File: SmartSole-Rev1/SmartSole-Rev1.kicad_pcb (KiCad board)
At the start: 2 copper layers, 37.4 x 68.6 mm, 33 parts, among them J1 5103310-5, J2 1-825433-2, J3 1-825433-2, U1 MCP6004, U2 MCP6004, U3 AD1583

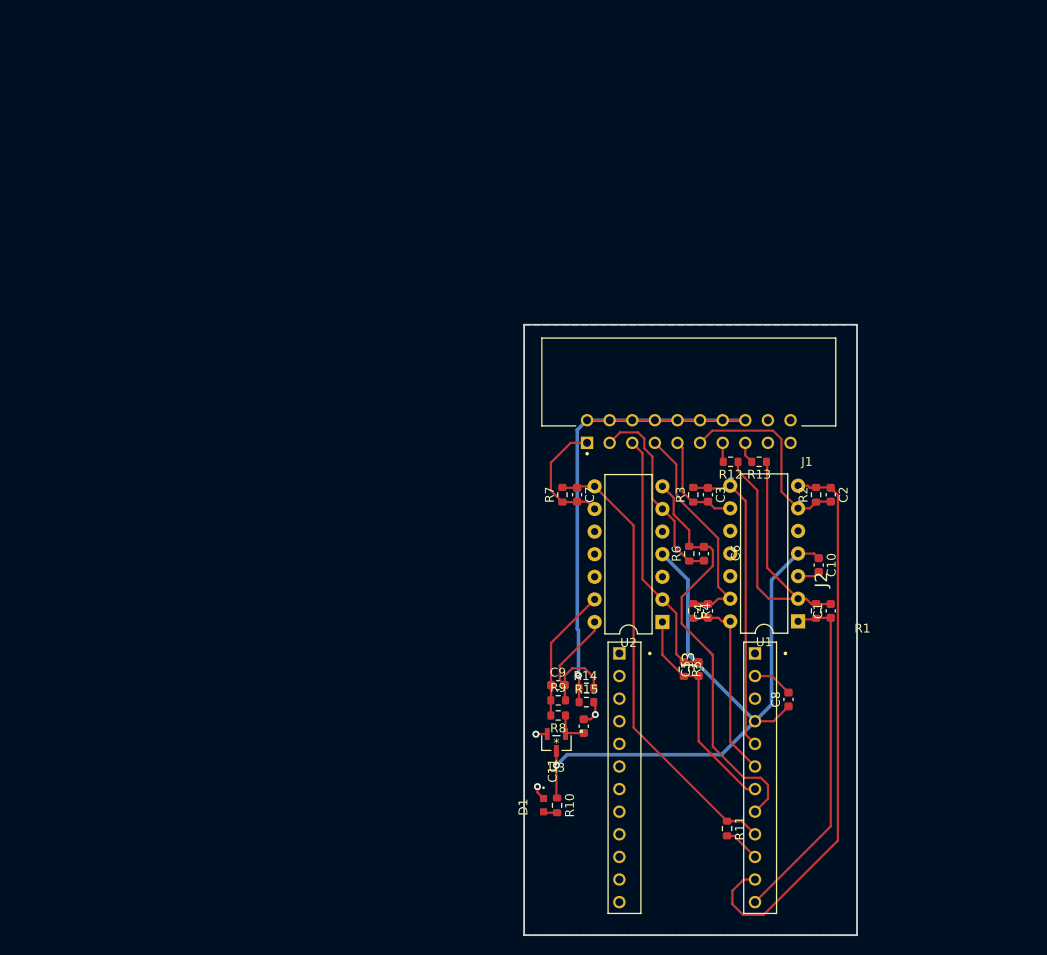
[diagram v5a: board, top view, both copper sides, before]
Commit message: Moved component ref silk screen, added board stackup + characteristics
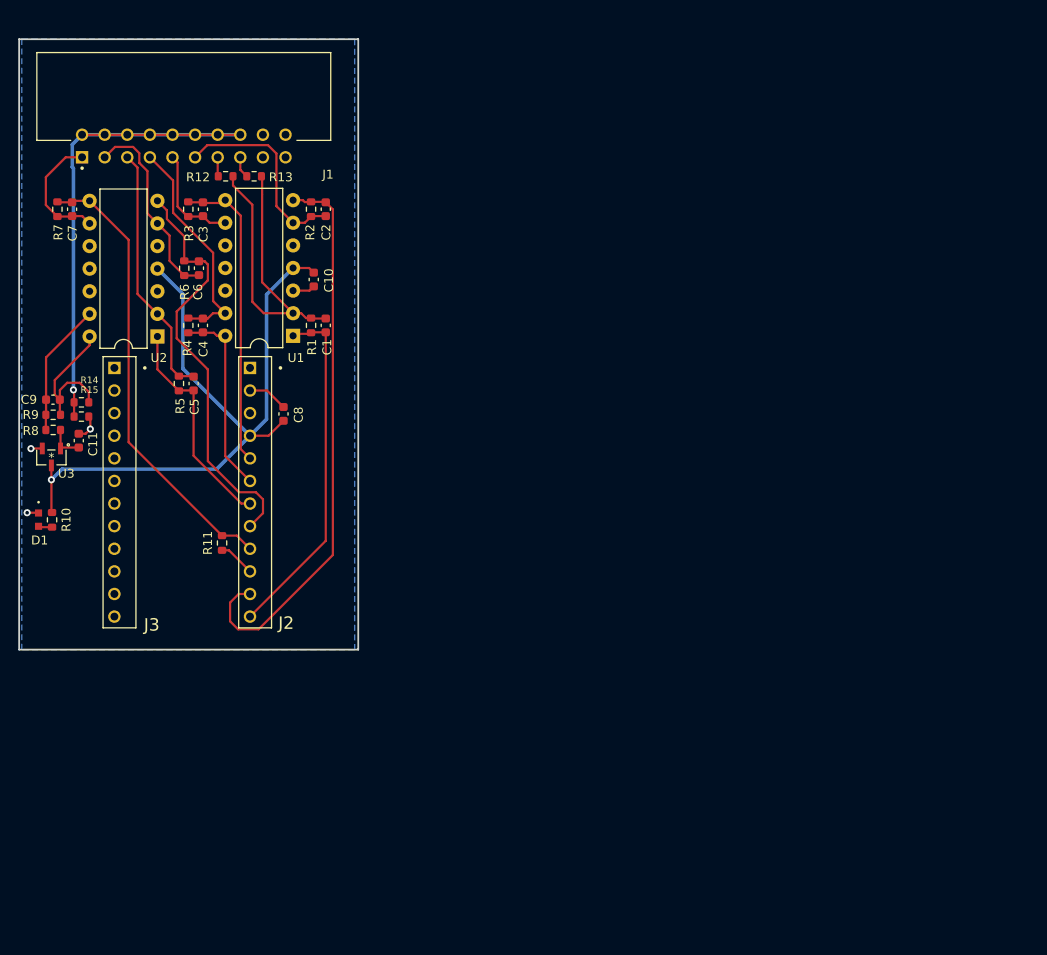
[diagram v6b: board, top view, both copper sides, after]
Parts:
- moved C10 65.2 mm to (92.7, 58.3)
- moved C7 65.2 mm to (65.5, 50.4)
- moved J1 65.2 mm to (78.1, 43.3)
- moved R2 65.2 mm to (92.4, 50.4)
- moved C1 65.2 mm to (94.0, 63.5)
- moved C11 65.2 mm to (66.3, 76.4)
- moved C2 65.2 mm to (94.0, 50.4)
- moved C3 65.2 mm to (80.2, 50.4)
- moved C4 65.2 mm to (80.2, 63.5)
- moved C6 65.2 mm to (79.8, 57.0)
- moved C8 65.2 mm to (89.3, 73.4)
- moved C9 65.2 mm to (63.4, 71.8)
- moved J2 65.2 mm to (85.5, 82.2)
- moved J3 65.2 mm to (70.3, 82.2)
- moved R1 65.2 mm to (92.4, 63.5)
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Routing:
- net /ForceIn_4: track 26.6 -> 25.4 mm
- net /AIN5: track 48.0 -> 47.4 mm
- net GND: track 12.9 -> 12.4 mm
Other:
- board size 37.4 x 68.6 mm -> 38.1 x 68.6 mm
- board text added: "0"
- board text added: "0 mils"
- board text added: "0.02"
- board text added: "0.3937008 mils"
- board text added: "1"
- board text added: "1.377953 mils"
- board text added: "11.81 mils"
- board text added: "1507.87 mils x 2707.87 mils"
- board text added: "2"
- board text added: "3.3"
- board text added: "4.5"
- board text added: "59.44882 mils"
- board text added: "6.00 mils / 6.00 mils"
- board text added: "62.99 mils"
- board text added: "B.Cu"
- board text added: "B.Mask"
- board text added: "B.Paste"
- board text added: "B.Silkscreen"
- board text added: "BOARD CHARACTERISTICS"
- board text added: "Board Thickness:"
- board text added: "Board overall dimensions:"
- board text added: "Bottom Silk Screen"
- board text added: "Bottom Solder Mask"
- board text added: "Bottom Solder Paste"
- board text added: "Castellated pads:"
- board text added: "Color"
- board text added: "Copper Finish:"
- board text added: "Copper Layer Count:"
- board text added: "Dielectric 1"
- board text added: "Edge card connectors:"
- board text added: "Epsilon R"
- board text added: "F.Cu"
- board text added: "F.Mask"
- board text added: "F.Paste"
- board text added: "F.Silkscreen"
- board text added: "FR4"
- board text added: "Impedance Control:"
- board text added: "Layer Name"
- board text added: "Loss Tangent"
- board text added: "Material"
- board text added: "Min hole diameter:"
- board text added: "Min track/spacing:"
- board text added: "No"
- board text added: "None"
- board text added: "Not specified"
- board text added: "Plated Board Edge:"
- board text added: "Thickness (mils)"
- board text added: "Top Silk Screen"
- board text added: "Top Solder Mask"
- board text added: "Top Solder Paste"
- board text added: "Type"
- board text added: "copper"
- board text added: "core"

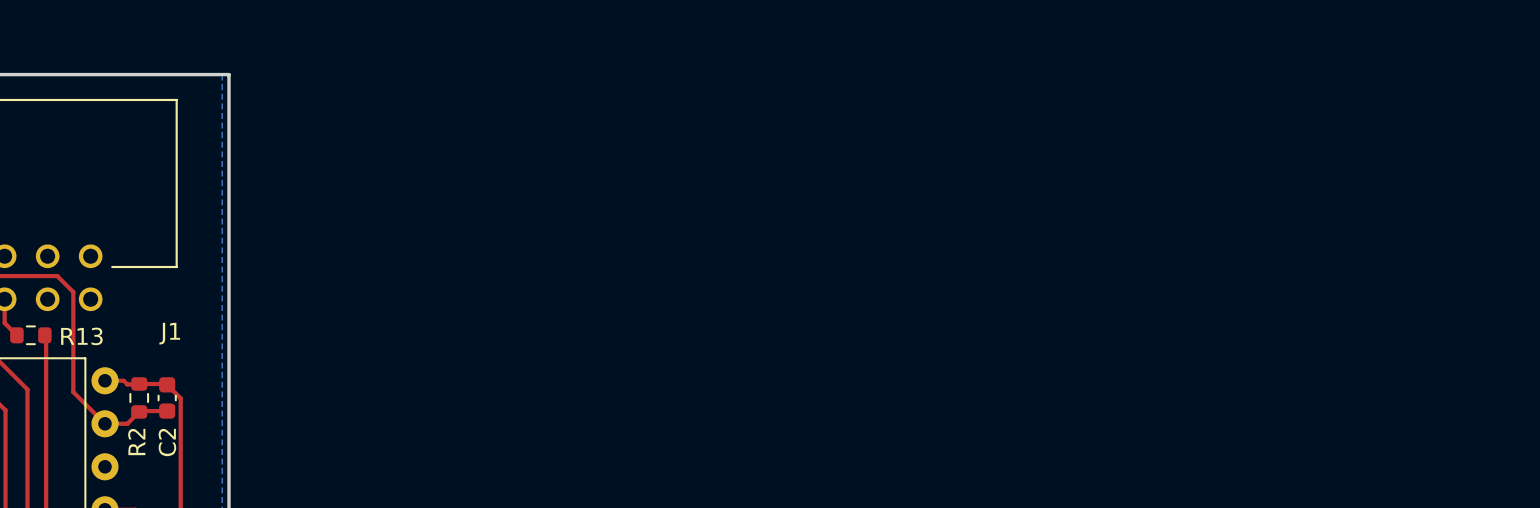
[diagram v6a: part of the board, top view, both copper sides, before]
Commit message: changed to non-inverting config
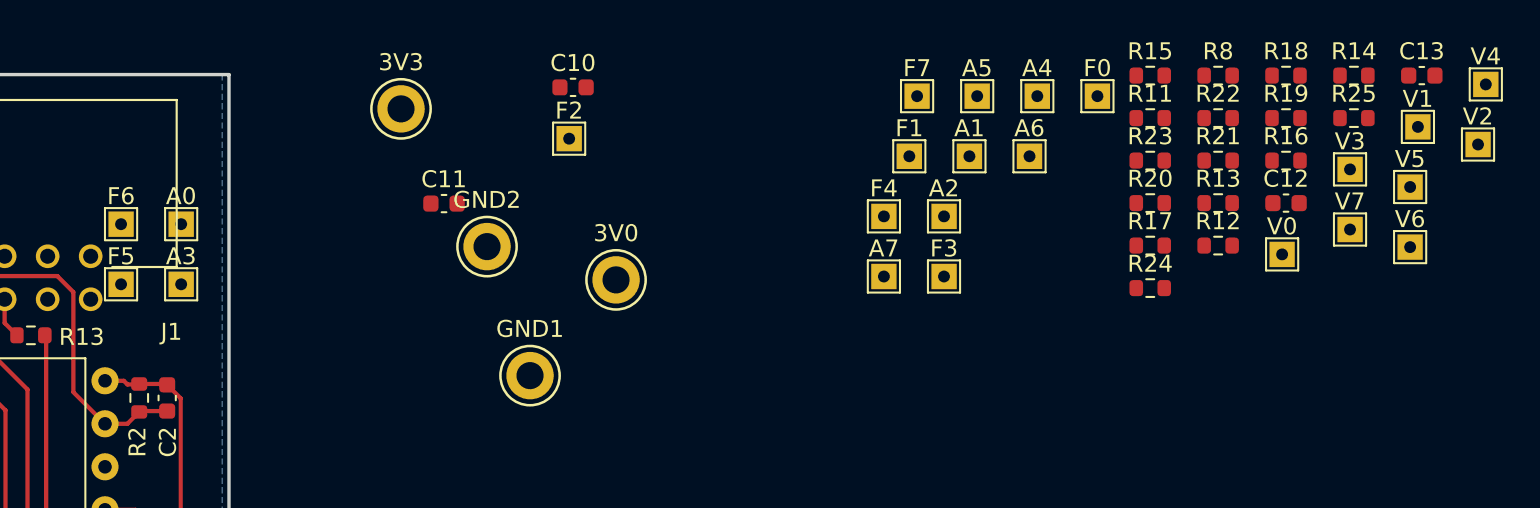
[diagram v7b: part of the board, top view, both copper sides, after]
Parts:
- added 3V0: 5005, TestPoint:TestPoint_Keystone_5005-5009_Compact, F.Cu at (120.5, 43.4)
- added 3V3: 5005, TestPoint:TestPoint_Keystone_5005-5009_Compact, F.Cu at (107.8, 33.3)
- added A0: TestPoint_Small, TestPoint:TestPoint_THTPad_1.5x1.5mm_Drill0.7mm, F.Cu at (94.8, 40.2)
- added A1: TestPoint_Small, TestPoint:TestPoint_THTPad_1.5x1.5mm_Drill0.7mm, F.Cu at (141.4, 36.1)
- added A2: TestPoint_Small, TestPoint:TestPoint_THTPad_1.5x1.5mm_Drill0.7mm, F.Cu at (139.9, 39.7)
- added A3: TestPoint_Small, TestPoint:TestPoint_THTPad_1.5x1.5mm_Drill0.7mm, F.Cu at (94.8, 43.7)
- added A4: TestPoint_Small, TestPoint:TestPoint_THTPad_1.5x1.5mm_Drill0.7mm, F.Cu at (145.4, 32.6)
- added A5: TestPoint_Small, TestPoint:TestPoint_THTPad_1.5x1.5mm_Drill0.7mm, F.Cu at (141.9, 32.6)
- added A6: TestPoint_Small, TestPoint:TestPoint_THTPad_1.5x1.5mm_Drill0.7mm, F.Cu at (144.9, 36.1)
- added A7: TestPoint_Small, TestPoint:TestPoint_THTPad_1.5x1.5mm_Drill0.7mm, F.Cu at (136.3, 43.2)
- added C10: 4.7uF, Capacitor_SMD:C_0603_1608Metric, F.Cu at (118.0, 32.1)
- added C11: 1uF, Capacitor_SMD:C_0603_1608Metric, F.Cu at (110.4, 38.9)
- added C12: 0.1uF, Capacitor_SMD:C_0603_1608Metric, F.Cu at (160.1, 38.9)
- added C13: 0.1uF, Capacitor_SMD:C_0603_1608Metric, F.Cu at (168.1, 31.4)
- added F0: TestPoint_Small, TestPoint:TestPoint_THTPad_1.5x1.5mm_Drill0.7mm, F.Cu at (149.0, 32.6)
- added F1: TestPoint_Small, TestPoint:TestPoint_THTPad_1.5x1.5mm_Drill0.7mm, F.Cu at (137.8, 36.1)
- added F2: TestPoint_Small, TestPoint:TestPoint_THTPad_1.5x1.5mm_Drill0.7mm, F.Cu at (117.8, 35.1)
- added F3: TestPoint_Small, TestPoint:TestPoint_THTPad_1.5x1.5mm_Drill0.7mm, F.Cu at (139.9, 43.2)
- added F4: TestPoint_Small, TestPoint:TestPoint_THTPad_1.5x1.5mm_Drill0.7mm, F.Cu at (136.3, 39.7)
- added F5: TestPoint_Small, TestPoint:TestPoint_THTPad_1.5x1.5mm_Drill0.7mm, F.Cu at (91.3, 43.7)
- added F6: TestPoint_Small, TestPoint:TestPoint_THTPad_1.5x1.5mm_Drill0.7mm, F.Cu at (91.3, 40.2)
- added F7: TestPoint_Small, TestPoint:TestPoint_THTPad_1.5x1.5mm_Drill0.7mm, F.Cu at (138.3, 32.6)
- added GND1: 5006, TestPoint:TestPoint_Keystone_5005-5009_Compact, F.Cu at (115.4, 49.1)
- added GND2: 5006, TestPoint:TestPoint_Keystone_5005-5009_Compact, F.Cu at (112.9, 41.5)
- added R11: R, Resistor_SMD:R_0603_1608Metric, F.Cu at (152.1, 33.9)
- added R12: R, Resistor_SMD:R_0603_1608Metric, F.Cu at (156.1, 41.4)
- added R13: R, Resistor_SMD:R_0603_1608Metric, F.Cu at (156.1, 38.9)
- added R14: R, Resistor_SMD:R_0603_1608Metric, F.Cu at (164.1, 31.4)
- added R15: R, Resistor_SMD:R_0603_1608Metric, F.Cu at (152.1, 31.4)
- added R16: R, Resistor_SMD:R_0603_1608Metric, F.Cu at (160.1, 36.4)
- added R17: R, Resistor_SMD:R_0603_1608Metric, F.Cu at (152.1, 41.4)
- added R18: R, Resistor_SMD:R_0603_1608Metric, F.Cu at (160.1, 31.4)
- added R19: R, Resistor_SMD:R_0603_1608Metric, F.Cu at (160.1, 33.9)
- added R20: R, Resistor_SMD:R_0603_1608Metric, F.Cu at (152.1, 38.9)
- added R21: R, Resistor_SMD:R_0603_1608Metric, F.Cu at (156.1, 36.4)
- added R22: R, Resistor_SMD:R_0603_1608Metric, F.Cu at (156.1, 33.9)
- added R23: R, Resistor_SMD:R_0603_1608Metric, F.Cu at (152.1, 36.4)
- added R24: R, Resistor_SMD:R_0603_1608Metric, F.Cu at (152.1, 43.9)
- added R25: R, Resistor_SMD:R_0603_1608Metric, F.Cu at (164.1, 33.9)
- added R8: R, Resistor_SMD:R_0603_1608Metric, F.Cu at (156.1, 31.4)
- added V0: TestPoint_Small, TestPoint:TestPoint_THTPad_1.5x1.5mm_Drill0.7mm, F.Cu at (159.9, 41.9)
- added V1: TestPoint_Small, TestPoint:TestPoint_THTPad_1.5x1.5mm_Drill0.7mm, F.Cu at (167.9, 34.4)
- added V2: TestPoint_Small, TestPoint:TestPoint_THTPad_1.5x1.5mm_Drill0.7mm, F.Cu at (171.4, 35.5)
- added V3: TestPoint_Small, TestPoint:TestPoint_THTPad_1.5x1.5mm_Drill0.7mm, F.Cu at (163.9, 36.9)
- added V4: TestPoint_Small, TestPoint:TestPoint_THTPad_1.5x1.5mm_Drill0.7mm, F.Cu at (171.9, 31.9)
- added V5: TestPoint_Small, TestPoint:TestPoint_THTPad_1.5x1.5mm_Drill0.7mm, F.Cu at (167.4, 38.0)
- added V6: TestPoint_Small, TestPoint:TestPoint_THTPad_1.5x1.5mm_Drill0.7mm, F.Cu at (167.4, 41.5)
- added V7: TestPoint_Small, TestPoint:TestPoint_THTPad_1.5x1.5mm_Drill0.7mm, F.Cu at (163.9, 40.5)
- C8: value 0.1u -> 1uF
- C9: value .01u -> 47pF
- R10: value 10k -> 68
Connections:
- C2 pad 2: /ForceIn_2 -> /ForceIn_1
- C3 pad 2: /ForceIn_3 -> /ForceIn_2
- C4 pad 2: /ForceIn_4 -> /ForceIn_3
- C5 pad 2: /ForceIn_5 -> /ForceIn_4
- C6 pad 2: /ForceIn_6 -> /ForceIn_5
- C7 pad 2: /ForceIn_7 -> /ForceIn_6
- C8 pad 1: /3.3V -> +3V3
- C9 pad 1: Net-(R8-Pad2) -> /ForceIn_7
- C9 pad 2: Net-(R9-Pad2) -> /AIN7
- J1 pad 10: /VRef -> GND
- J1 pad 12: /VRef -> GND
- J1 pad 13: Net-(J1-Pad13) -> /ForceIn_1
- J1 pad 14: /VRef -> GND
- J1 pad 15: Net-(J1-Pad15) -> /ForceIn_0
- J1 pad 16: /VRef -> GND
- J1 pad 17: unconnected-(J1-Pad17) -> GND
- J1 pad 18: unconnected-(J1-Pad18) -> GND
- J1 pad 19: unconnected-(J1-Pad19) -> GND
- J1 pad 2: /VRef -> GND
- J1 pad 20: unconnected-(J1-Pad20) -> GND
- J1 pad 4: /VRef -> GND
- J1 pad 6: /VRef -> GND
- J1 pad 8: /VRef -> GND
- J2 pad 10: Net-(J2-Pad10) -> /AIN7
- J2 pad 4: /3.3V -> +3V3
- R10 pad 1: /3.3V -> +3V3
- R2 pad 1: /ForceIn_2 -> /ForceIn_1
- R3 pad 1: /ForceIn_3 -> /ForceIn_2
- R4 pad 1: /ForceIn_4 -> /ForceIn_3
- R5 pad 1: /ForceIn_5 -> /ForceIn_4
- R6 pad 1: /ForceIn_6 -> /ForceIn_5
- R7 pad 1: /ForceIn_7 -> /ForceIn_6
- R9 pad 1: Net-(R8-Pad2) -> /ForceIn_7
- R9 pad 2: Net-(R9-Pad2) -> /AIN7
- U1 pad 10: GND -> /Op Amps/VRef2
- U1 pad 12: GND -> /Op Amps/VRef3
- U1 pad 13: /ForceIn_4 -> /ForceIn_3
- U1 pad 3: GND -> /Op Amps/VRef0
- U1 pad 4: /3.3V -> +3V3
- U1 pad 5: GND -> /Op Amps/VRef1
- U1 pad 6: /ForceIn_2 -> /ForceIn_1
- U1 pad 9: /ForceIn_3 -> /ForceIn_2
- U2 pad 10: GND -> /Op Amps/VRef6
- U2 pad 12: GND -> /Op Amps/VRef7
- U2 pad 13: Net-(R8-Pad2) -> /ForceIn_7
- U2 pad 14: Net-(R9-Pad2) -> /AIN7
- U2 pad 2: /ForceIn_5 -> /ForceIn_4
- U2 pad 3: GND -> /Op Amps/VRef4
- U2 pad 4: /3.3V -> +3V3
- U2 pad 5: GND -> /Op Amps/VRef5
- U2 pad 6: /ForceIn_6 -> /ForceIn_5
- U2 pad 9: /ForceIn_7 -> /ForceIn_6
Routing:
- net /3.3V: track 80.6 -> 0.00 mm, vias 1 -> 0
- net +3V3: track 0.00 -> 80.6 mm, vias 0 -> 1
- net /VRef: track 67.8 -> 0.00 mm
- net GND: track 12.4 -> 80.1 mm
- net /ForceIn_1: track 0.00 -> 22.6 mm
- net Net-(R9-Pad2): track 17.0 -> 0.00 mm
- net /AIN7: track 0.00 -> 17.0 mm
- net Net-(R8-Pad2): track 15.1 -> 0.00 mm
- net /ForceIn_3: track 11.8 -> 25.4 mm
- net /ForceIn_2: track 22.6 -> 11.8 mm
- net /ForceIn_6: track 22.2 -> 13.9 mm
- net /ForceIn_5: track 28.7 -> 22.2 mm
- net /ForceIn_4: track 25.4 -> 28.7 mm
- net /ForceIn_7: track 13.9 -> 15.1 mm

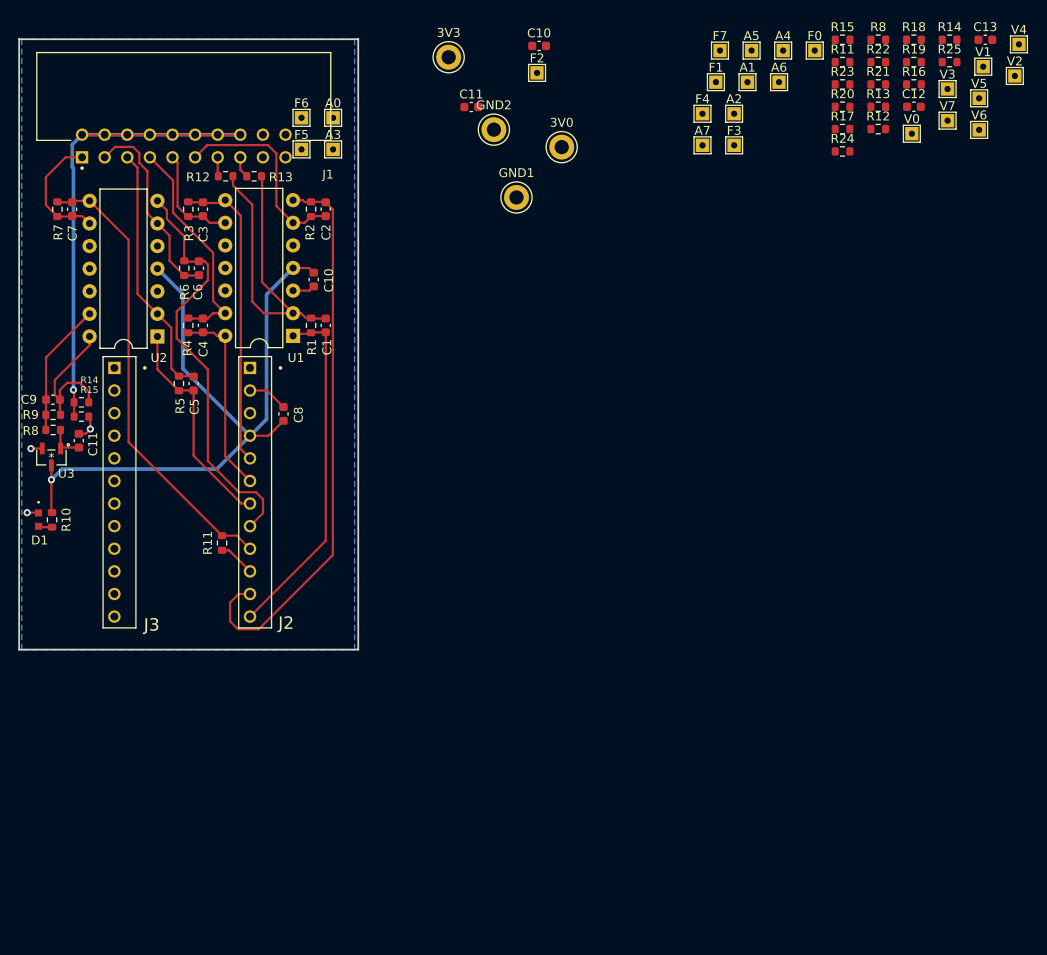
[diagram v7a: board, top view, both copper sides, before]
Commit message: changed to single coltage reference per opamp IC
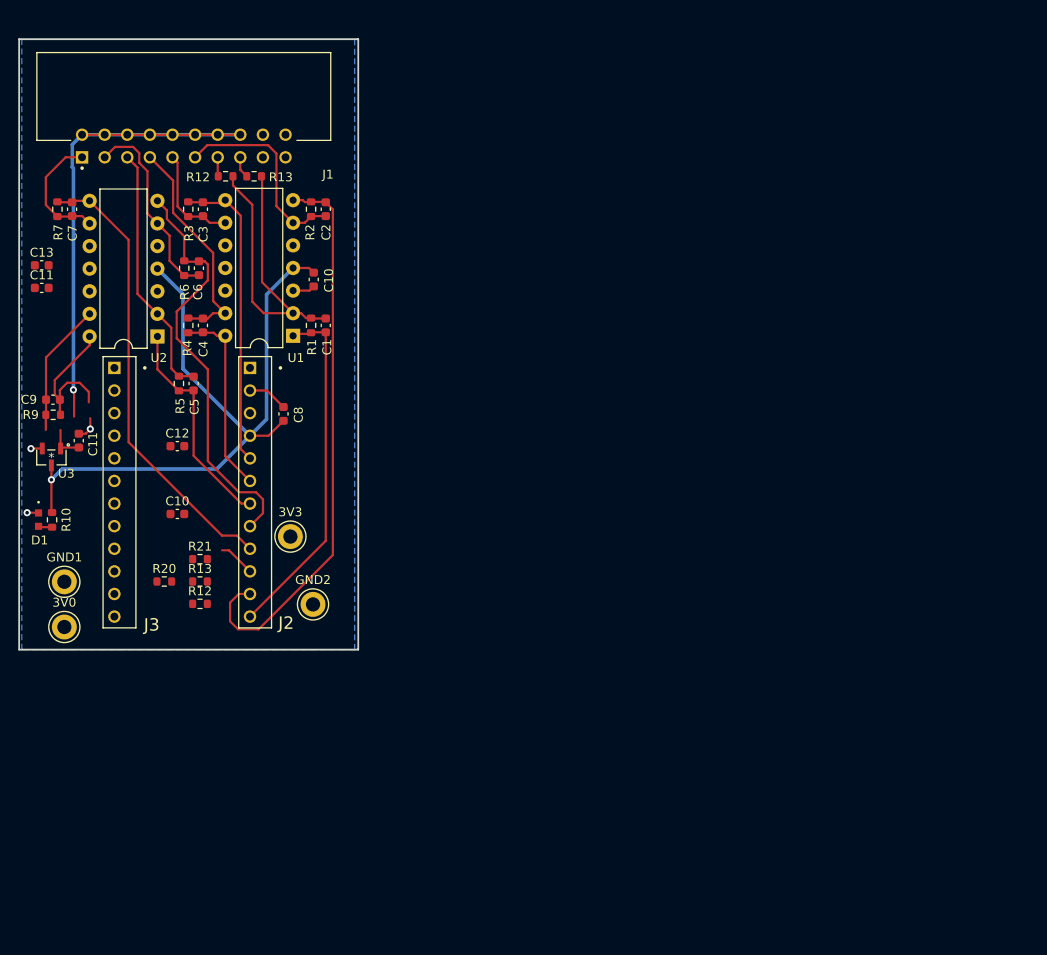
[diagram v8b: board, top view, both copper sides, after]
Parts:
- removed A0, A1, A2, A3, A4, A5, A6, A7, F0, F1, F2, F3, F4, F5, F6, F7, V0, V1, V2, V3, V4, V5, V6, V7: TestPoint_Small, TestPoint:TestPoint_THTPad_1.5x1.5mm_Drill0.7mm
- removed R11, R15: 0 - DNP, Resistor_SMD:R_0603_1608Metric
- removed R11, R14, R15, R16, R17, R18, R19, R22, R23, R24, R25, R8: R, Resistor_SMD:R_0603_1608Metric
- removed R14: 0, Resistor_SMD:R_0603_1608Metric
- removed R8: 680, Resistor_SMD:R_0603_1608Metric
- C10: value 4.7u -> 4.7uF
- C11: value 1u -> 1uF
- R12: value 0 -> R
- R13: value 0 - DNP -> R
- moved C13 109.0 mm to (62.1, 56.7)
- moved R12 93.0 mm to (79.9, 94.8)
- moved R13 93.0 mm to (79.9, 92.2)
- moved R21 93.0 mm to (79.9, 89.7)
- moved R20 93.0 mm to (75.9, 92.2)
- moved C12 91.1 mm to (77.3, 77.0)
- moved 3V0 77.6 mm to (64.6, 97.4)
- moved GND1 66.7 mm to (64.6, 92.3)
- moved C10 66.5 mm to (77.3, 84.7)
- moved GND2 57.1 mm to (92.6, 94.8)
- moved 3V3 56.7 mm to (90.0, 87.2)
- moved C11 52.4 mm to (62.1, 59.3)
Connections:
- C10 pad 1: /3.3V -> +3V3
- C11 pad 1: Net-(R8-Pad1) -> /VRef
- R12 pad 2: /Op Amps/VRef0 -> /Op Amps/VRef1
- R12 pad 1: /ForceIn_0 -> /VRef
- R12 pad 2: Net-(J1-Pad13) -> /Op Amps/VRef1
- R13 pad 1: /ForceIn_0 -> /Op Amps/VRef1
- R13 pad 2: Net-(J1-Pad15) -> GND
- R13 pad 1: /Op Amps/VRef0 -> /Op Amps/VRef1
- R20 pad 2: /Op Amps/VRef4 -> /Op Amps/VRef2
- R21 pad 1: /Op Amps/VRef4 -> /Op Amps/VRef2
- U1 pad 10: /Op Amps/VRef2 -> /Op Amps/VRef1
- U1 pad 12: /Op Amps/VRef3 -> /Op Amps/VRef1
- U1 pad 3: /Op Amps/VRef0 -> /Op Amps/VRef1
- U2 pad 10: /Op Amps/VRef6 -> /Op Amps/VRef2
- U2 pad 12: /Op Amps/VRef7 -> /Op Amps/VRef2
- U2 pad 3: /Op Amps/VRef4 -> /Op Amps/VRef2
- U2 pad 5: /Op Amps/VRef5 -> /Op Amps/VRef2
- U3 pad 1: Net-(R8-Pad1) -> /VRef
- U3 pad 3: /3.3V -> +3V3
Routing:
- net Net-(R8-Pad1): track 4.18 -> 0.00 mm
- net /VRef: track 0.00 -> 4.18 mm
- net Net-(J2-Pad10): track 4.12 -> 0.00 mm
- net /AIN7: track 17.0 -> 21.1 mm
- net GND: track 80.1 -> 82.6 mm
- net Net-(J1-Pad15): track 2.43 -> 0.00 mm
- net Net-(J1-Pad13): track 2.16 -> 0.00 mm
- net /Op Amps/VRef1: track 0.00 -> 2.16 mm
